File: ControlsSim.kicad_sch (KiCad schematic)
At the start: 26 parts, among them J2 Accelerator Pot, J3 Brake Button, J5 Motor Contactors, J6 Array Contactors, J7 Rotary Switch, SW2 SW_Rotary2x6

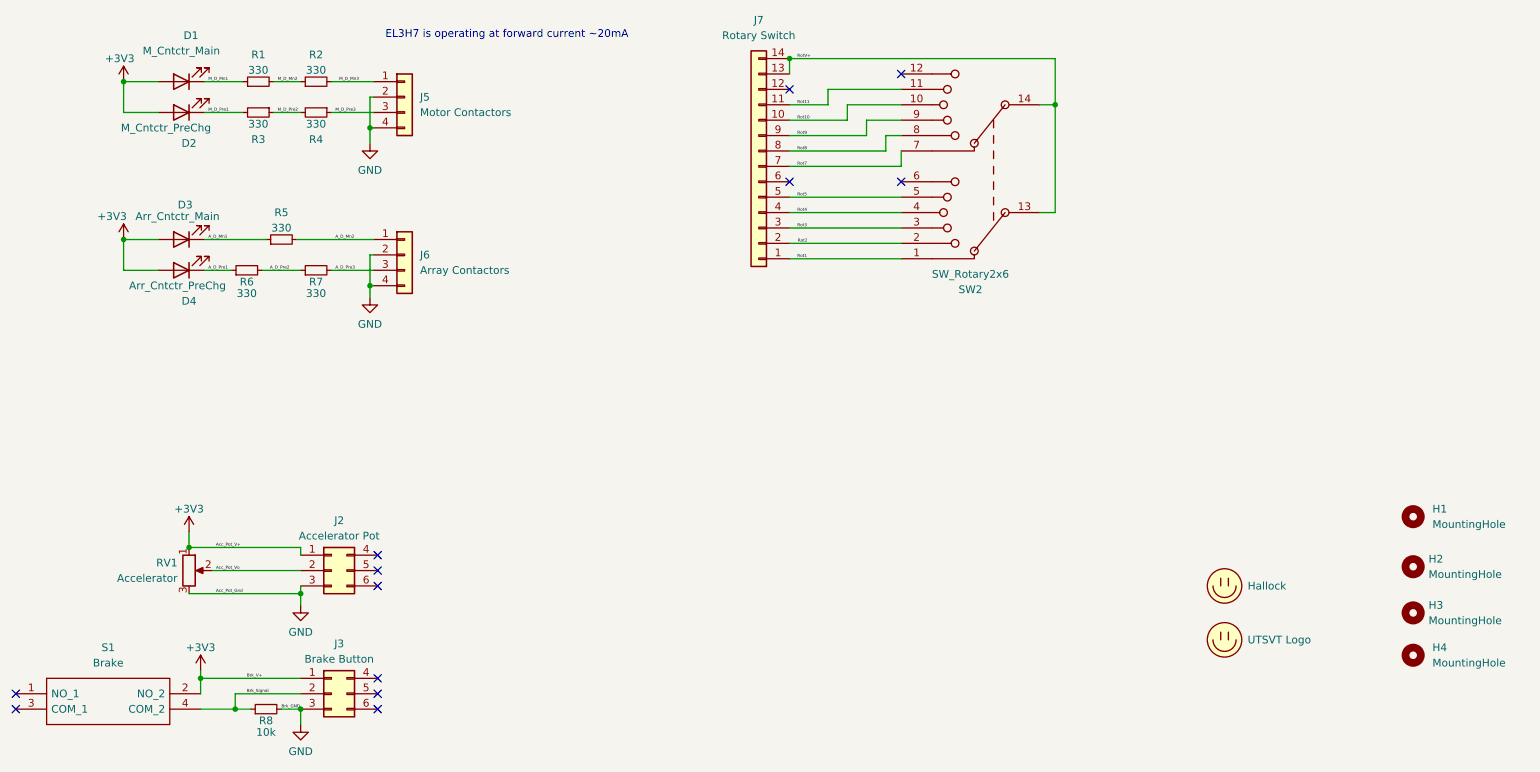
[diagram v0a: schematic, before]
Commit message: Fixed Submodule, added Version History, and fixed folder organization
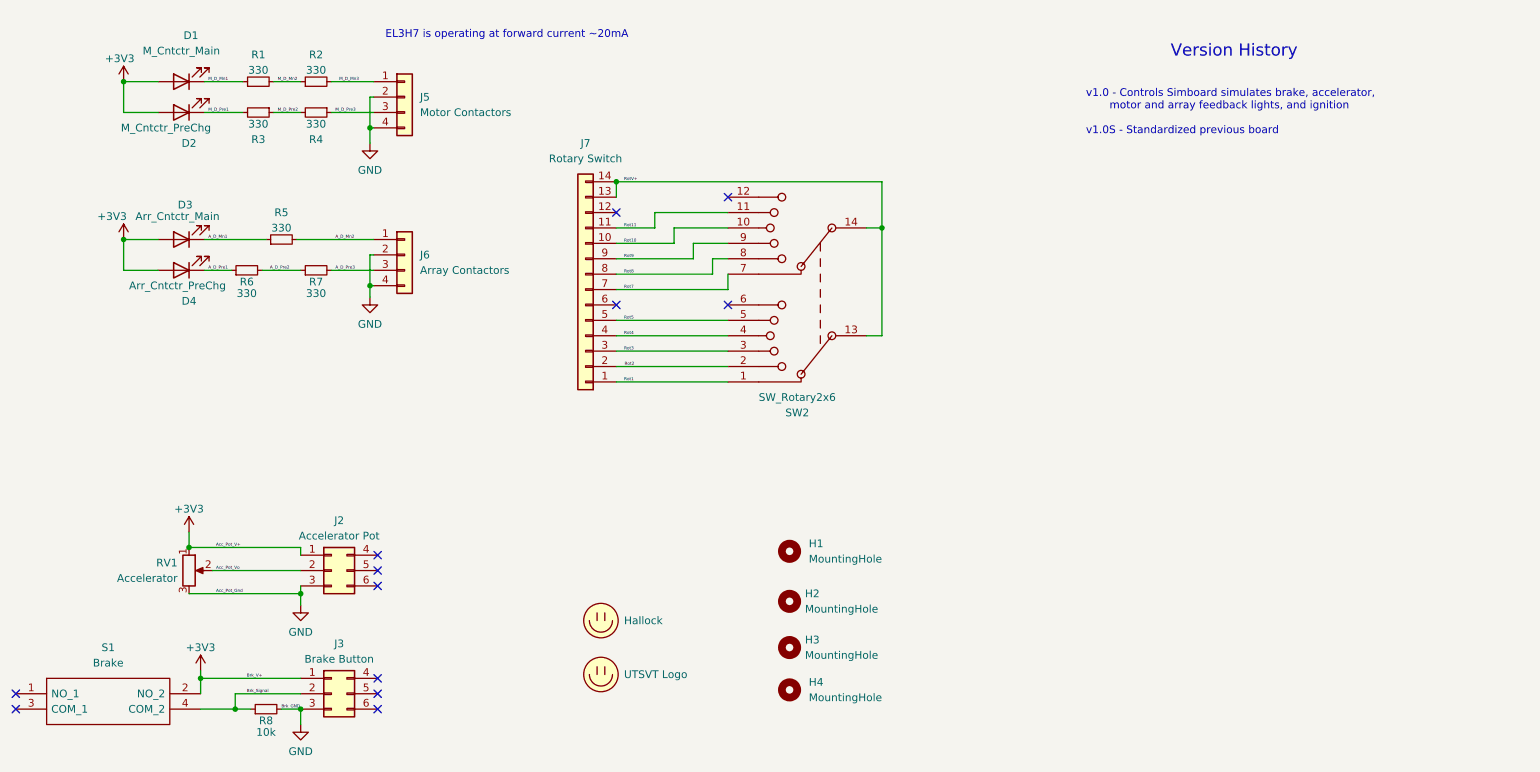
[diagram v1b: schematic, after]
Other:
- note added: "Version History"
- note added: "v1.0 - Controls Simboard simulates brake, accelerator, motor and array feedback lights, and ignition v1.0S - Standardized previous board"
- moved on the sheet: H1, H2, H3, H4, J7, SW2
